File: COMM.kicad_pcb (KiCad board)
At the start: 4 copper layers, 90.2 x 95.9 mm, 37 parts, among them IC1 Voltage Converter (ADP7158ARD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, J1 SMA Conn. (RFPC-SMA30-F), SW1 Inhibit Switch (SS5GLD2), U1 XBee Module (XBP9B-DMSTB002), U2 AX.25 Module (DMR818SU)

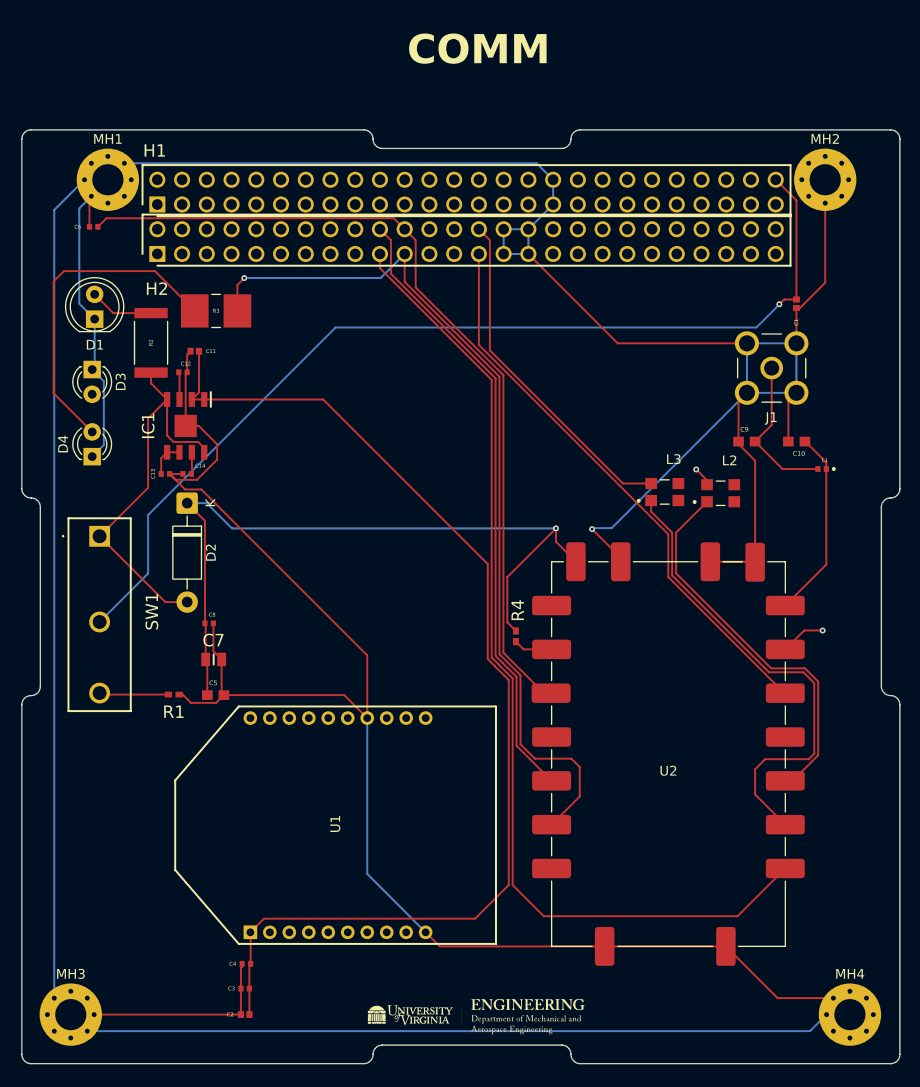
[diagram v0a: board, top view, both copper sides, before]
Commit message: Finalized board design, updated DMR module to DMR818S-5W exact dimensions, rerouted PCB according to McPherson's comments. Added TLV61047 5V to 8V booster module.
Signed-off-by: Logan Tolbert <xem6df@virginia.edu>
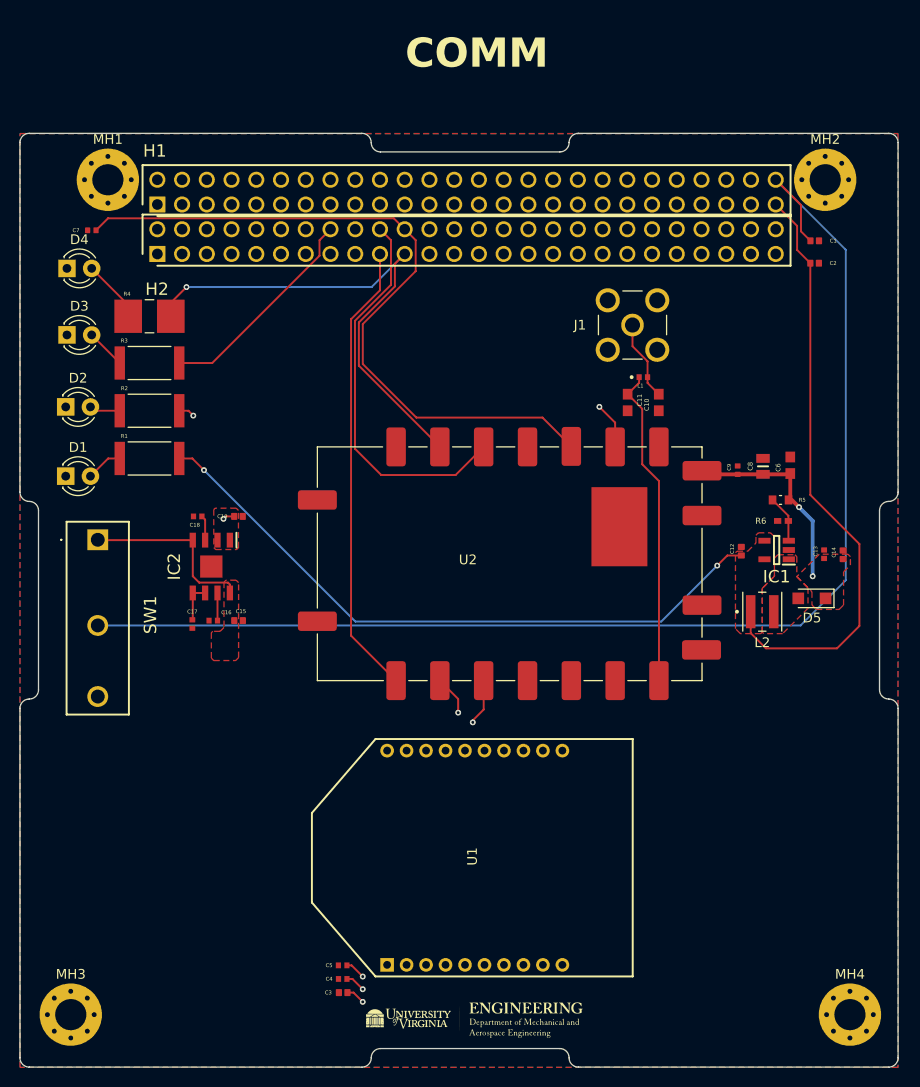
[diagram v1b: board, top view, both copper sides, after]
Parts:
- removed the D2 at (118.8, 91.3)
- removed L3: 200 nH, CLT32_R20_200nH:IND_CLT32-R20
- removed the R4 at (152.5, 105.0)
- added C12: 10 μF, C_10uF:CAPC1005X70N, F.Cu at (175.7, 96.2)
- added C13: 1 μF, C_1uF:CAPC1005X55N, F.Cu at (184.2, 96.5)
- added C14: 10 μF, C_10uF:CAPC1005X70N, F.Cu at (186.1, 96.6)
- added C15: 10 μF, C_10uF:CAPC1005X70N, F.Cu at (124.0, 103.3)
- added C2: 10 μF, C_10uF:CAPC1005X70N, F.Cu at (183.2, 66.7)
- added D1: GRN_DMR, LED_THT:LED_D3.0mm, F.Cu at (106.3, 88.5)
- added D5: PMEG3020BER, Diode_SMD:Nexperia_CFP3_SOD-123W, F.Cu at (182.9, 101.1)
- added IC1: TLV61047DDCR, TLV61047:SOT95P280X110-5N, F.Cu at (179.3, 96.1)
- added R3: 140 Ω, R_470O:RESC6332X65N, F.Cu at (114.9, 76.9)
- added R5: 53.6 kΩ, R_53.6kO:RESC1608X55N, F.Cu at (179.7, 91.0)
- added R6: 10 kΩ, R_10kO:RESC1005X40N, F.Cu at (180.0, 93.1)
- D2: renamed from D1; value LED -> GRN_XB; footprint LED_THT:LED_D5.0mm -> LED_THT:LED_D3.0mm
- D3: value LED -> YLW_ASC_XB
- D4: value LED -> BLU_TR_DMR
- L2: value 200 nH -> 10 μH; footprint CLT32_R20_200nH:IND_CLT32-R20 -> L_10uH_frt:IND_XAL4040-103MEC
- R1: value 10 kΩ -> 130 Ω; footprint R_10kO:RESC1005X40N -> R_470O:RESC6332X65N
- R2: value 470 Ω -> 130 Ω
- R4: renamed from R3; value 220 Ω -> 80 Ω
- U2: value AX.25 Module (DMR818SU) -> DMR Module (DMR818S-5W); footprint DMR818S:DMR818SU -> DMR818S:DMR818S-5W
- moved C6 63.6 mm to (180.7, 87.4), turned to 90 degrees
- moved C8 59.8 mm to (177.9, 87.5), turned to 90 degrees
- moved C9 56.5 mm to (175.3, 87.9), turned to 90 degrees
- moved U2 33.9 mm to (168.4, 83.2), turned to -90 degrees
- moved R1 24.4 mm to (114.9, 86.7), turned to 0 degrees
- moved L1 20.6 mm to (165.6, 78.3), turned to 180 degrees
- moved D4 19.5 mm to (106.4, 67.2), turned to 0 degrees
- moved C11 17.8 mm to (164.0, 81.0), turned to -90 degrees
- moved C19 17.5 mm to (124.0, 92.7), turned to 0 degrees
- moved C17 15.7 mm to (119.3, 103.7), turned to -90 degrees
- moved C16 15.3 mm to (121.5, 103.3)
- moved J1 15.0 mm to (164.5, 73.0)
- moved C18 14.9 mm to (119.8, 92.7), turned to 180 degrees
- moved IC2 14.7 mm to (121.2, 97.8)
- moved U1 14.4 mm to (148.1, 127.7)
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- renumbered C9 to C10, C10 to C11, C14 to C16, C13 to C17, C12 to C18, C11 to C19, C2 to C3, C3 to C4, C4 to C5, C5 to C6, C6 to C7, C7 to C8, C8 to C9, IC1 to IC2
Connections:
- net /DMR818S-U 2W RF Module/ANT renamed /DMR818S 5W RF Module/ANT
- net /DMR818S-U 2W RF Module/VCC renamed +8V
- D3 pad 2: /Associate/DIO5_XB -> Net-(D3-A)
- H1 pad 51: unconnected-(H1-Pad51) -> /TLV61047/VIN
- H2 pad 25: /HST_RXD_DMR -> unconnected-(H2-Pad25)
- H2 pad 27: /HST_TXD_DMR -> unconnected-(H2-Pad27)
- IC2 pad 4: /Voltage Converter XB/VIN -> /Voltage Converter/VIN
- IC2 pad 8: /Voltage Converter XB/VIN -> /Voltage Converter/VIN
- L2 pad 1: Net-(U2-UART_RX) -> /TLV61047/VIN
- L2 pad 2: /UART_RX_DMR -> Net-(D5-A)
- R1 pad 1: GND -> Net-(D1-A)
- R1 pad 2: Net-(SW1-C) -> /TLV61047/VIN
- R2 pad 2: /Voltage Converter XB/VIN -> +3.3V
- SW1 pad 1: /Voltage Converter XB/VIN -> /Voltage Converter/VIN
- SW1 pad 3: Net-(SW1-C) -> unconnected-(SW1-C-Pad3)
- U2 pad 13: Net-(U2-CS) -> +3.3V
- U2 pad 2: Net-(U2-UART_TX) -> /UART_TX_DMR
- U2 pad 3: Net-(U2-UART_RX) -> /UART_RX_DMR
- U2 pad 5: /HST_TXD_DMR -> unconnected-(U2-HST_TXD-Pad5)
- U2 pad 6: /HST_RXD_DMR -> unconnected-(U2-HST_RXD-Pad6)
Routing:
- net GND: track 546.4 -> 0.00 mm, vias 1 -> 0
- net /TLV61047/VIN: track 0.00 -> 129.3 mm, vias 0 -> 2
- net +3.3V: track 113.6 -> 13.8 mm, vias 0 -> 6
- net /HST_RXD_DMR: track 59.0 -> 0.00 mm, vias 1 -> 0
- net /HST_TXD_DMR: track 58.2 -> 0.00 mm
- net +8V: track 76.8 -> 21.8 mm, vias 1 -> 2
- net /MIC_IN_DMR: track 101.8 -> 47.0 mm
- net Net-(U2-UART_TX): track 48.7 -> 0.00 mm
- net /Voltage Converter XB/VIN: track 40.6 -> 0.00 mm
- net Net-(U2-UART_RX): track 39.9 -> 0.00 mm
- net /T/R_DMR: track 90.6 -> 52.7 mm
- net /Associate/DIO5_XB: track 121.5 -> 87.2 mm
- net +5V: track 102.0 -> 130.6 mm, vias 1 -> 0
- net Net-(D4-A): track 33.7 -> 6.47 mm
- net /LINE_OUT_DMR: track 63.9 -> 40.1 mm
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- added copper zone on B.Cu, net +3.3V
- added copper zone on F.Cu, net +3.3V
- added copper zone on F.Cu, net +8V
- added copper zone on F.Cu, net /TLV61047/VIN
- added copper zone on F.Cu, net /Voltage Converter/VIN
- added copper zone on F.Cu, net GND
- added copper zone on F.Cu, net Net-(D5-A)

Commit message: Modified traces
Signed-off-by: Logan Tolbert <xem6df@virginia.edu>
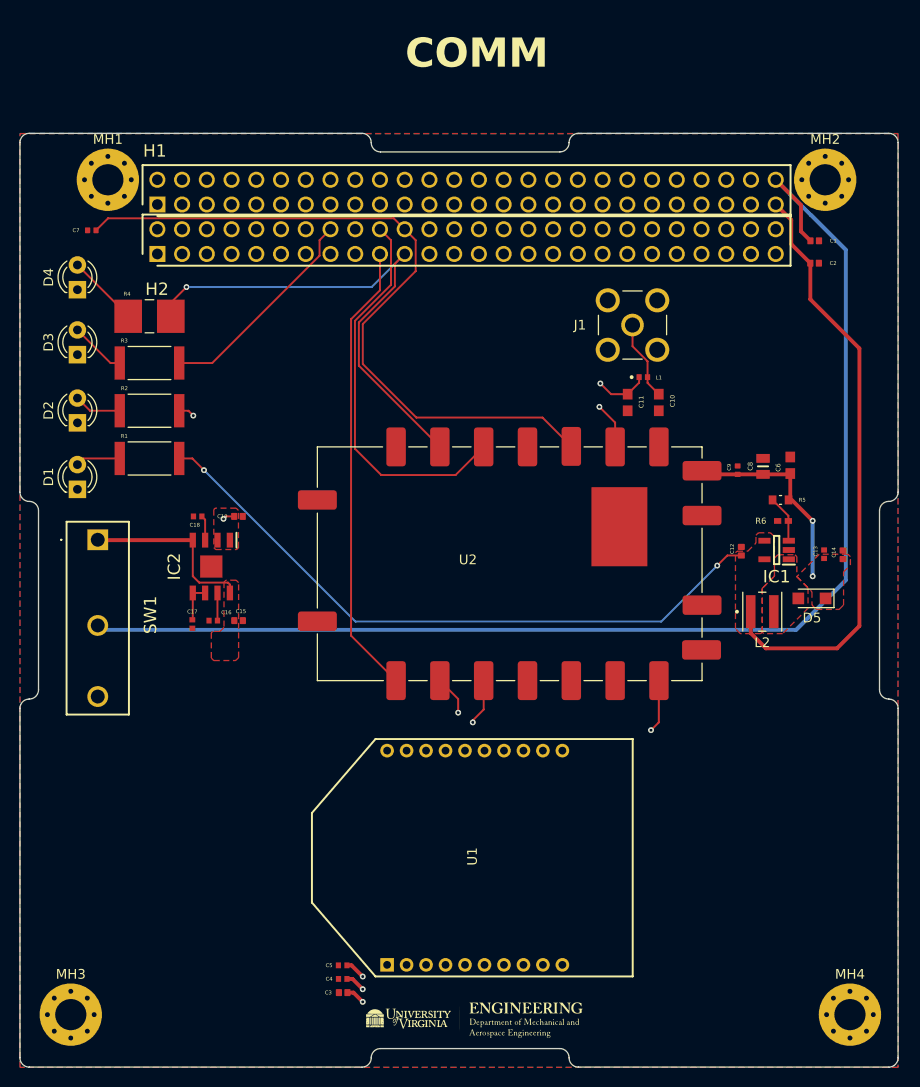
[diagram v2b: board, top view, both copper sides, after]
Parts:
- moved D4 2.44 mm to (107.5, 69.4), turned to 90 degrees
- moved D3 2.29 mm to (107.5, 76.0), turned to 90 degrees
- moved D2 2.03 mm to (107.5, 83.0), turned to 90 degrees
- moved D1 1.81 mm to (107.5, 89.9), turned to 90 degrees
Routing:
- net Net-(U2-ANT): track 33.0 -> 48.7 mm, vias 0 -> 2
- net Net-(D4-A): track 6.47 -> 8.60 mm
- net Net-(D2-A): track 3.17 -> 4.88 mm
- net Net-(D3-A): track 4.08 -> 5.76 mm
- net Net-(D1-A): track 3.76 -> 4.61 mm
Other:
- rule pad_to_mask_clearance: 0 -> 0.0508

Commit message: Removed extranous capacitors and resistors off of DMR module. Final Board Design, check one more time before ordering parts.
Signed-off-by: Logan Tolbert <xem6df@virginia.edu>
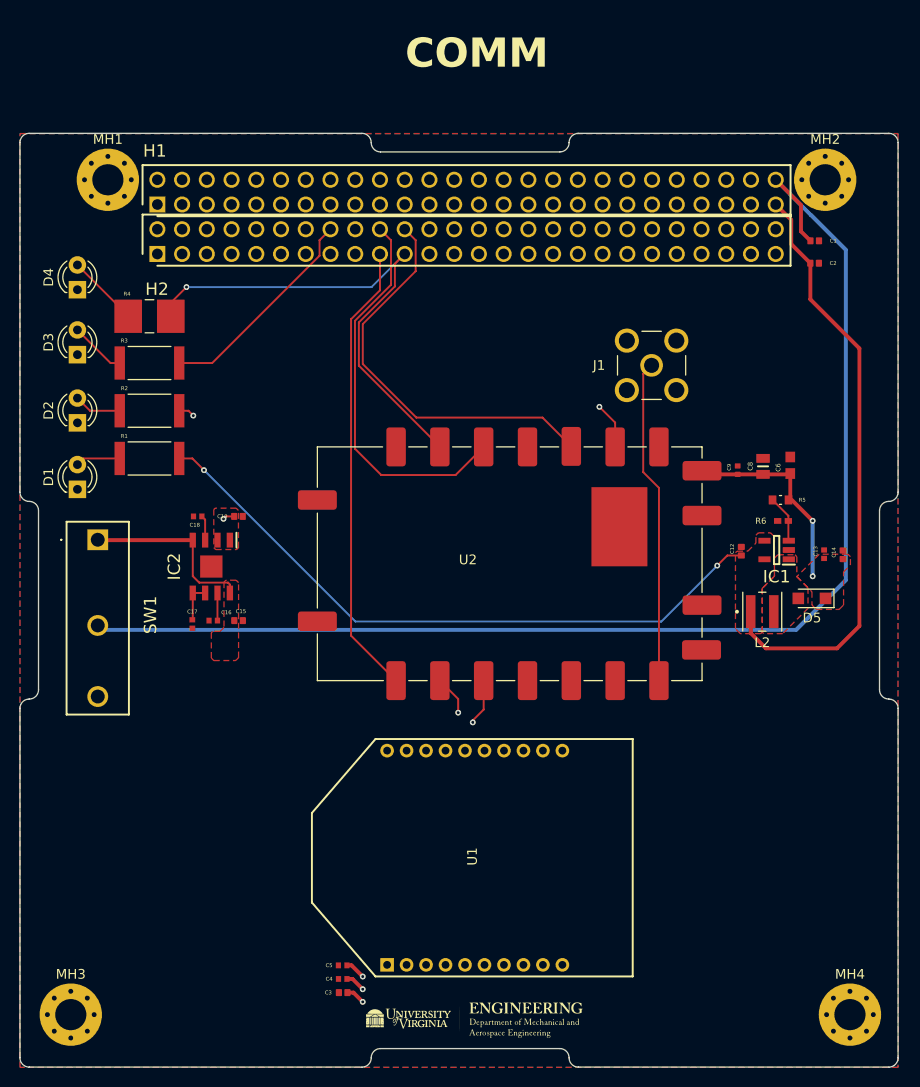
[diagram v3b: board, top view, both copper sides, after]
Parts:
- removed C10, C11: 100 nF, C_100nF:CAPC1608X90
- removed C7: 100 pF, C_100pF:CAPC1005X55N
- removed L1: 18 nH, LQG15HS18NJ02D_18nH:INDC1005X55N
- moved J1 4.58 mm to (166.5, 77.1)
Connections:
- U2 pad 7: Net-(U2-ANT) -> /DMR818S 5W RF Module/ANT
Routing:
- net Net-(U2-ANT): track 48.7 -> 0.00 mm, vias 2 -> 0
- net /PTT_DMR: track 74.2 -> 41.5 mm
- net /DMR818S 5W RF Module/ANT: track 8.22 -> 33.4 mm

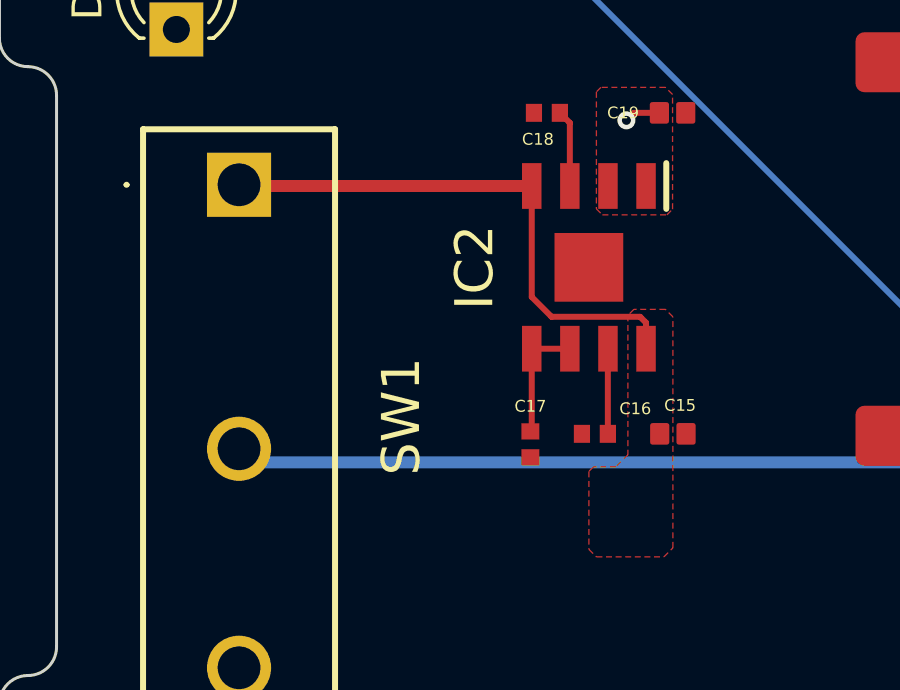
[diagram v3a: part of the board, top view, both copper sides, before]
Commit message: Modified 5V trace from switch to voltage step-down module
Signed-off-by: Logan Tolbert <xem6df@virginia.edu>
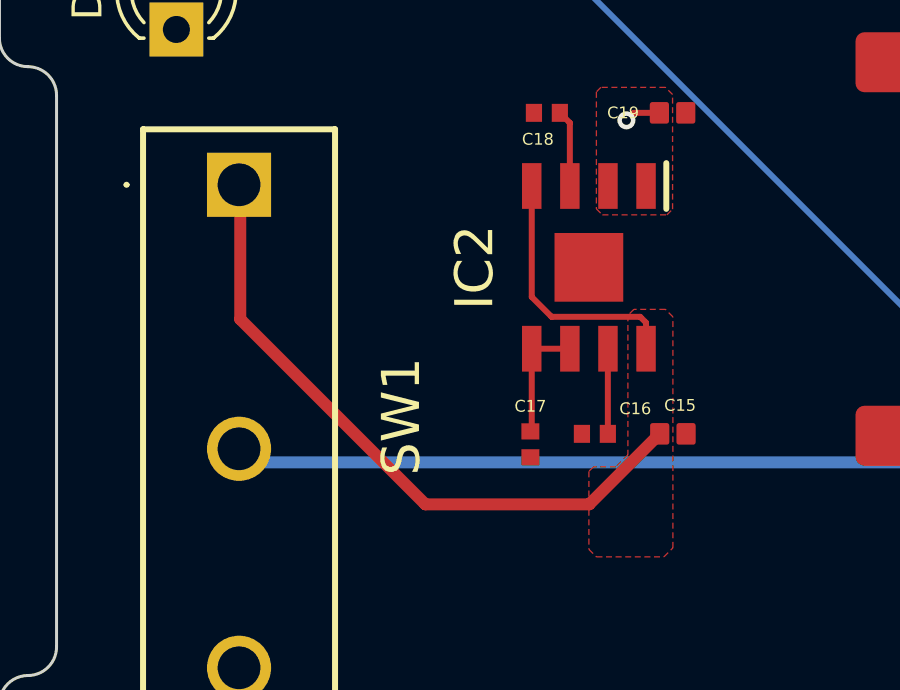
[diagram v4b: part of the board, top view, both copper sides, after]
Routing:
- net /Voltage Converter/VIN: track 18.5 -> 30.7 mm
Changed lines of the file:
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@@
 	)
 	(segment
-		(start 119.345 95.088)
-		(end 109.629081 95.088)
+		(start 115.8 105.7)
+		(end 121.261 105.7)
 		(width 0.4)
 		(layer "F.Cu")
@@
 	)
 	(segment
+		(start 109.629081 99.529081)
+		(end 115.8 105.7)
+		(width 0.4)
+		(layer "F.Cu")
+		(net 28)
+	)
+	(segment
 		(start 109.629081 95.088)
 		(end 109.5883 95.047219)
@@
 	)
 	(segment
+		(start 121.261 105.7)
+		(end 123.611 103.35)
+		(width 0.4)
+		(layer "F.Cu")
+		(net 28)
+	)
+	(segment
 		(start 119.345 95.088)
 		(end 119.345 98.787)
@@
 		(layer "F.Cu")
 		(net 28)
+	)
+	(segment
+		(start 109.629081 95.088)
+		(end 109.629081 99.529081)
+		(width 0.4)
+		(layer "F.Cu")
+		(net 28)

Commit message: Final COMM board design as of Feb 12 2026, ready to order.
Signed-off-by: Logan Tolbert <xem6df@virginia.edu>
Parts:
- removed SW1: Inhibit Switch (SS5GLD2), Inhibit_Switch_COMM:SS5GLD2
- added S1: SS-5GLD2, Inhibit_Switch_COMM:SS5GLD2, F.Cu at (109.5, 95.0)
- D1: value GRN_DMR -> GRN_8V
- D3: renamed from D2; value GRN_XB -> RED_3V3
- D4: value BLU_TR_DMR -> YLW_TR_DMR
- D5: footprint Diode_SMD:Nexperia_CFP3_SOD-123W -> PMEG3020BER_115:DIODE_SOD123W_1P9X2P8_NEX
- R1: value 130 Ω -> 250 Ω; footprint R_470O:RESC6332X65N -> R_250O:RESC2012X65N
- R2: renamed from R3; footprint R_470O:RESC6332X65N -> R_140O:RESC3216X70N
- R3: renamed from R2; value 130 Ω -> 110 Ω; footprint R_470O:RESC6332X65N -> R_110O:RESC1508X55N
- R4: value 80 Ω -> 140 Ω; footprint R_220O:RESC6332X70N -> R_140O:RESC3216X70N
- renumbered C13 to C10, C14 to C11, C15 to C12, C16 to C13, C17 to C14, C18 to C15, C19 to C16, C8 to C7, C9 to C8, C12 to C9, D3 to D2, L2 to L1
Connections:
- R1 pad 2: /TLV61047/VIN -> +8V
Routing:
- net +8V: track 21.8 -> 97.8 mm, vias 2 -> 3
- net /TLV61047/VIN: track 129.3 -> 61.8 mm, vias 2 -> 0
- net /Voltage Converter/VIN: track 30.7 -> 26.1 mm
- net +5V: track 131.0 -> 134.7 mm
- net +3.3V: track 13.8 -> 16.1 mm
- net Net-(D3-A): track 4.88 -> 7.18 mm
- net Net-(D1-A): track 4.61 -> 6.73 mm
- net /Associate/DIO5_XB: track 87.2 -> 88.8 mm
- net Net-(D2-A): track 5.76 -> 7.34 mm
